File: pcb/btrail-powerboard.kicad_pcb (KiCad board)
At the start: 2 copper layers, 42.5 x 36.5 mm, 13 parts, among them J1 RJ45_Shielded, Q1 BC328, Q2 BC328

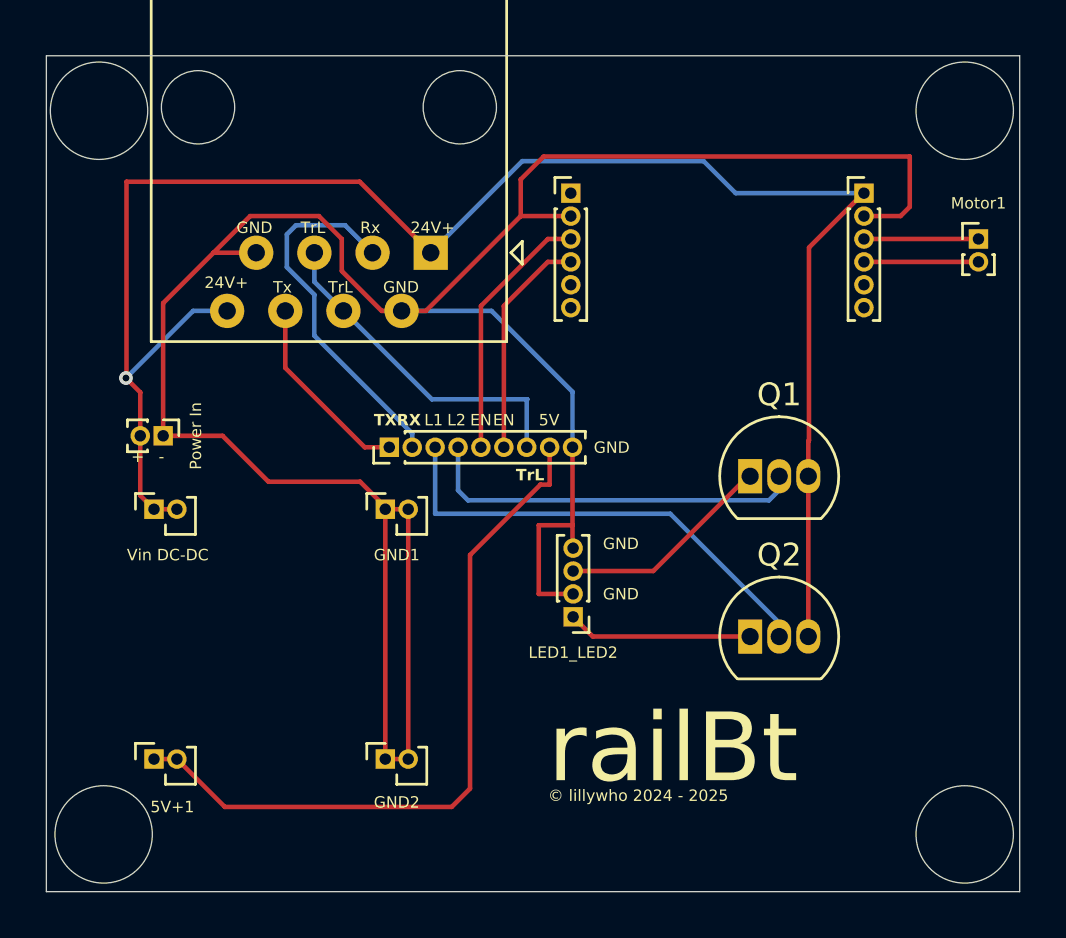
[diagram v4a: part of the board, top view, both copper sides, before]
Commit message: Update PCB to latest revision
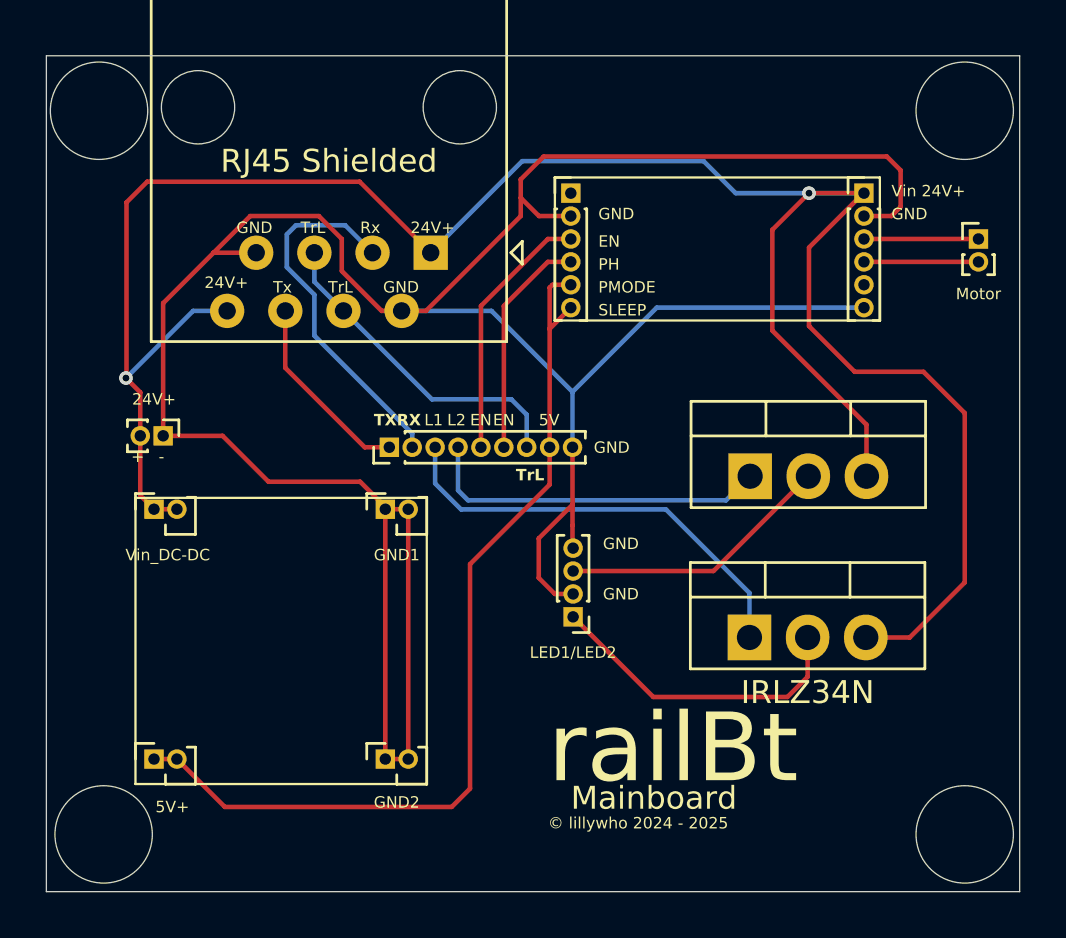
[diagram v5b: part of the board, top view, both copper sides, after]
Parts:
- removed Q2: BC328, Package_TO_SOT_THT:TO-92_Inline
- added IRLZ34N: IRLZ34N, Package_TO_SOT_THT:TO-220-3_Vertical, F.Cu at (220.2, 47.4)
- 24V+: renamed from Power In
- J1: value RJ45_Shielded -> RJ45 Shielded
- Q1: value BC328 -> IRLZ34N; footprint Package_TO_SOT_THT:TO-92_Inline -> Package_TO_SOT_THT:TO-220-3_Vertical
- Vin_DC-DC: renamed from Vin DC-DC
- renumbered 5V+1 to 5V+, LED1_LED2 to LED1/LED2, Motor1 to Motor
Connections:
- DRV_left1 pad 5: unconnected-(DRV_left1-Pin_5-Pad5) -> Net-(5V+1-Pin_1)
- DRV_left1 pad 6: unconnected-(DRV_left1-Pin_6-Pad6) -> Net-(5V+1-Pin_1)
- DRV_right1 pad 6: unconnected-(DRV_right1-Pin_6-Pad6) -> Net-(DRV_left1-Pin_2)
- LED1/LED2 pad 3: Net-(LED1_LED2-Pin_3) -> Net-(LED1/LED2-Pin_3)
- Q1 pad 1: Net-(LED1_LED2-Pin_3) -> Net-(ESP32_jack1-Pin_4)
- Q1 pad 2: Net-(ESP32_jack1-Pin_4) -> Net-(LED1/LED2-Pin_3)
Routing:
- net Net-(DRV_right1-Pin_1): track 77.6 -> 101.7 mm, vias 1 -> 2
- net Net-(DRV_left1-Pin_2): track 111.4 -> 124.5 mm
- net Net-(LED1/LED2-Pin_3): track 0.00 -> 12.0 mm
- net Net-(LED1_LED2-Pin_3): track 9.44 -> 0.00 mm
- net Net-(5V+1-Pin_1): track 31.6 -> 40.6 mm
- net Net-(LED1/LED2-Pin_1): track 8.09 -> 13.8 mm
- net Net-(ESP32_jack1-Pin_4): track 16.9 -> 15.3 mm
- net Net-(ESP32_jack1-Pin_3): track 20.5 -> 19.3 mm
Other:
- board text added: "Mainboard"
- board text added: "PH"
- board text added: "PMODE"
- board text added: "SLEEP"
- board text added: "Vin 24V+"

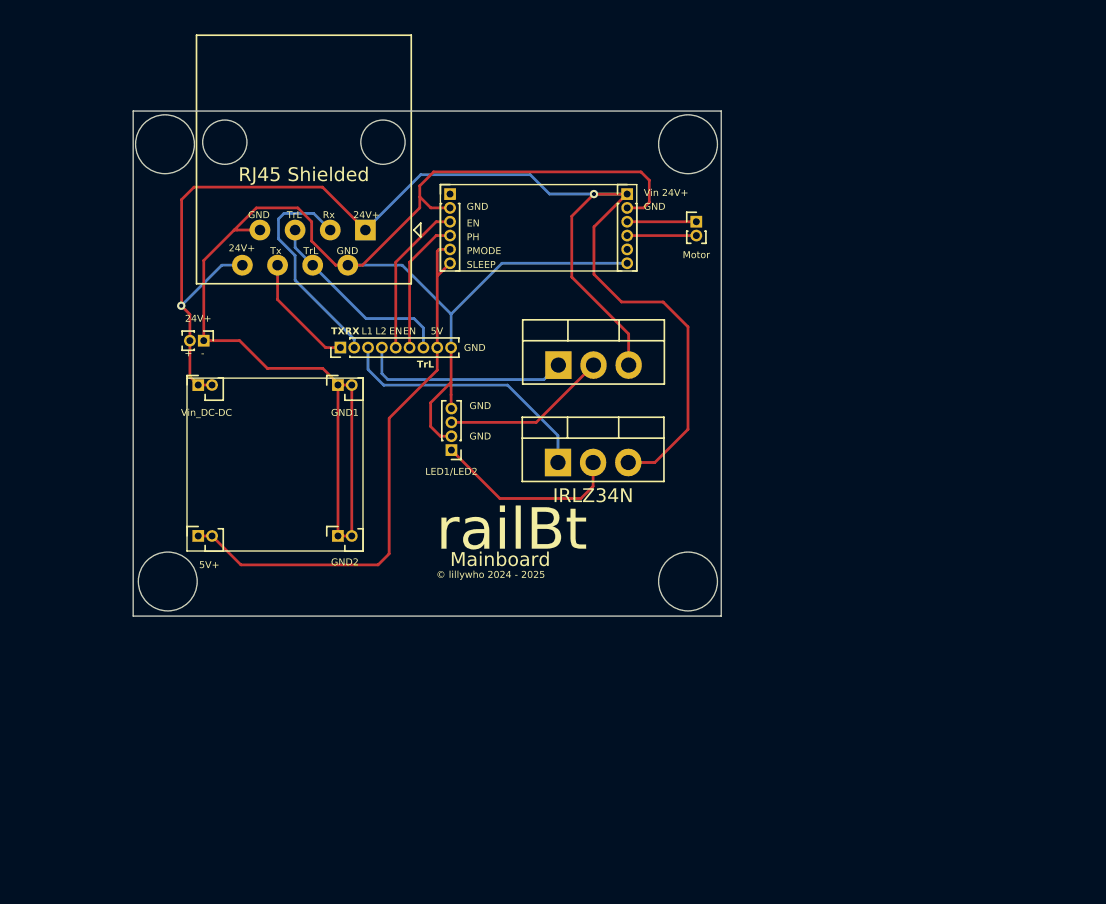
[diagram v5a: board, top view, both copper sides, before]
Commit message: Fix mainboard through hole and screw hole sizes
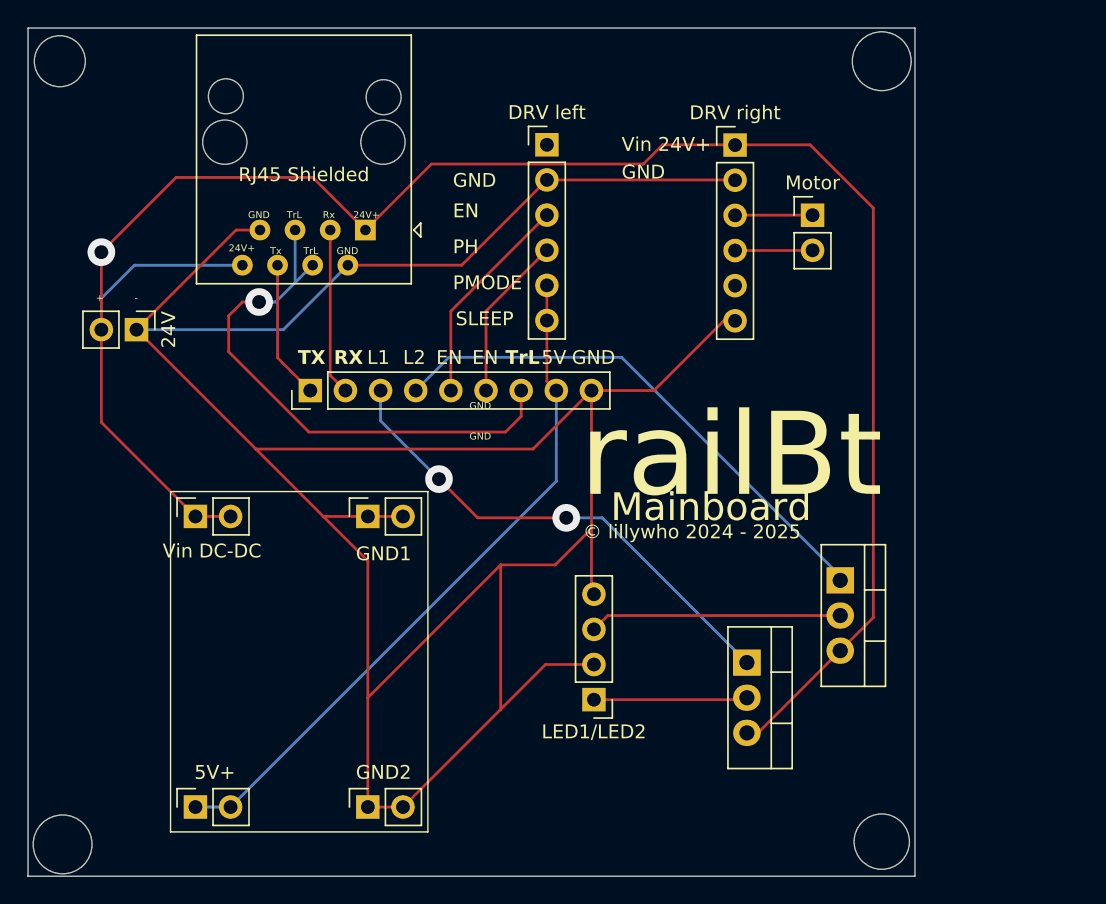
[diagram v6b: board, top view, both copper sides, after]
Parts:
- 24V: renamed from 24V+; footprint Connector_PinHeader_1.00mm:PinHeader_1x02_P1.00mm_Vertical -> Connector_PinHeader_2.54mm:PinHeader_1x02_P2.54mm_Vertical
- 5V+, GND1, GND2: footprint Connector_PinSocket_1.00mm:PinSocket_1x02_P1.00mm_Vertical -> Connector_PinSocket_2.54mm:PinSocket_1x02_P2.54mm_Vertical
- DRV left: renamed from DRV_left1; footprint Connector_PinHeader_1.00mm:PinHeader_1x06_P1.00mm_Vertical -> Connector_PinHeader_2.54mm:PinHeader_1x06_P2.54mm_Vertical
- DRV right: renamed from DRV_right1; footprint Connector_PinHeader_1.00mm:PinHeader_1x06_P1.00mm_Vertical -> Connector_PinHeader_2.54mm:PinHeader_1x06_P2.54mm_Vertical
- ESP32_jack1: footprint Connector_PinHeader_1.00mm:PinHeader_1x09_P1.00mm_Vertical -> Connector_PinHeader_2.54mm:PinHeader_1x09_P2.54mm_Vertical
- LED1/LED2: footprint Connector_PinHeader_1.00mm:PinHeader_1x04_P1.00mm_Vertical -> Connector_PinHeader_2.54mm:PinHeader_1x04_P2.54mm_Vertical
- Motor: footprint Connector_PinHeader_1.00mm:PinHeader_1x02_P1.00mm_Vertical -> Connector_PinHeader_2.54mm:PinHeader_1x02_P2.54mm_Vertical
- Vin DC-DC: renamed from Vin_DC-DC; footprint Connector_PinSocket_1.00mm:PinSocket_1x02_P1.00mm_Vertical -> Connector_PinSocket_2.54mm:PinSocket_1x02_P2.54mm_Vertical
- moved Q1 25.6 mm to (240.6, 55.9), turned to -90 degrees
- moved LED1/LED2 20.8 mm to (222.8, 64.5)
- moved IRLZ34N 19.9 mm to (233.9, 61.9), turned to -90 degrees
- moved GND2 19.7 mm to (206.5, 72.3)
- moved 5V+ 19.6 mm to (194.0, 72.3)
- moved GND1 9.74 mm to (206.5, 51.3)
- moved Vin DC-DC 9.50 mm to (194.0, 51.3)
- moved DRV right 8.57 mm to (233.0, 24.5)
- moved Motor 8.41 mm to (238.6, 29.5)
- moved DRV left 7.85 mm to (219.4, 24.4)
- moved 24V 4.92 mm to (189.7, 37.8)
- moved ESP32_jack1 3.79 mm to (202.3, 42.2)
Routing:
- net Net-(DRV_left1-Pin_2): track 124.5 -> 212.4 mm
- net Net-(DRV_right1-Pin_1): track 101.7 -> 144.1 mm, vias 2 -> 1
- net Net-(ESP32_jack1-Pin_7): track 14.4 -> 39.9 mm, vias 0 -> 1
- net Net-(ESP32_jack1-Pin_4): track 15.3 -> 38.5 mm
- net Net-(ESP32_jack1-Pin_3): track 19.3 -> 35.9 mm, vias 0 -> 2
- net Net-(5V+1-Pin_1): track 40.6 -> 50.3 mm
- net Net-(LED1/LED2-Pin_3): track 12.0 -> 18.2 mm
- net Net-(DRV_left1-Pin_3): track 11.3 -> 15.6 mm
- net Net-(ESP32_jack1-Pin_2): track 16.0 -> 12.1 mm
- net Net-(LED1/LED2-Pin_1): track 13.8 -> 10.7 mm
- net Net-(DRV_left1-Pin_4): track 9.89 -> 12.0 mm
- net Net-(ESP32_jack1-Pin_1): track 8.47 -> 10.0 mm
- net Net-(DRV_right1-Pin_4): track 5.00 -> 5.61 mm
- net Net-(DRV_right1-Pin_3): track 5.00 -> 5.61 mm
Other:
- board size 42.5 x 36.5 mm -> 64.1 x 61.3 mm

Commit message: Final revision, added ground plane and more compact design, thanks Emily!
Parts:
- removed 24V, Motor: Conn_01x02_Pin, Connector_PinHeader_2.54mm:PinHeader_1x02_P2.54mm_Vertical
- added 24V In: Conn_01x02_Pin, Connector_PinHeader_2.54mm:PinHeader_1x02_P2.54mm_Vertical, F.Cu at (195.4, 40.7)
- added Motor1: Conn_01x02_Pin, Connector_PinHeader_2.54mm:PinHeader_1x02_P2.54mm_Vertical, F.Cu at (231.2, 29.6)
- DRV8874_left1: renamed from DRV left
- DRV8874_right1: renamed from DRV right
- J1: value RJ45 Shielded -> RJ45_Shielded
- Vin_DC-DC1: renamed from Vin DC-DC
- moved Q1 10.1 mm to (230.5, 56.0)
- moved Q2 8.35 mm to (225.6, 60.9)
- moved DRV8874_left1 5.53 mm to (213.9, 24.3)
- moved DRV8874_right1 5.53 mm to (227.5, 24.4)
- moved 5V+1 4.49 mm to (196.4, 68.5)
- moved GND1 4.49 mm to (208.9, 47.5)
- moved GND2 4.49 mm to (208.9, 68.5)
- moved Vin_DC-DC1 4.49 mm to (196.4, 47.5)
- moved LED1/LED2 2.60 mm to (220.2, 64.6)
- moved J1 1.78 mm to (207.5, 31.9)
- moved ESP32_jack1 1.10 mm to (201.2, 42.2)
- renumbered 5V+ to 5V+1, IRLZ34N to Q2
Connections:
- net Net-(5V+1-Pin_1) renamed +5V
- net Net-(DRV_left1-Pin_2) renamed GND
- net Net-(DRV_right1-Pin_1) renamed +24V
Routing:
- net GND: track 212.4 -> 0.00 mm
- net +24V: track 144.1 -> 133.3 mm, vias 1 -> 0
- net Net-(ESP32_jack1-Pin_2): track 12.1 -> 19.7 mm
- net Net-(LED1/LED2-Pin_3): track 18.2 -> 10.8 mm
- net Net-(ESP32_jack1-Pin_7): track 39.9 -> 33.5 mm
- net Net-(LED1/LED2-Pin_1): track 10.7 -> 5.83 mm
- net +5V: track 50.3 -> 54.2 mm
- net Net-(ESP32_jack1-Pin_4): track 38.5 -> 36.0 mm
- net Net-(ESP32_jack1-Pin_1): track 10.0 -> 7.78 mm
- net Net-(DRV8874_right1-Pin_4): track 5.61 -> 3.58 mm
- net Net-(DRV8874_right1-Pin_3): track 5.61 -> 3.58 mm
- net Net-(ESP32_jack1-Pin_3): track 35.9 -> 34.0 mm
- net Net-(DRV8874_left1-Pin_3): track 15.6 -> 13.9 mm
- added copper zone on B.Cu, net GND
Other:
- board size 64.1 x 61.3 mm -> 44.5 x 52.8 mm
